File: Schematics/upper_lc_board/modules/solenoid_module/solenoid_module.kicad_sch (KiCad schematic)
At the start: 8 parts

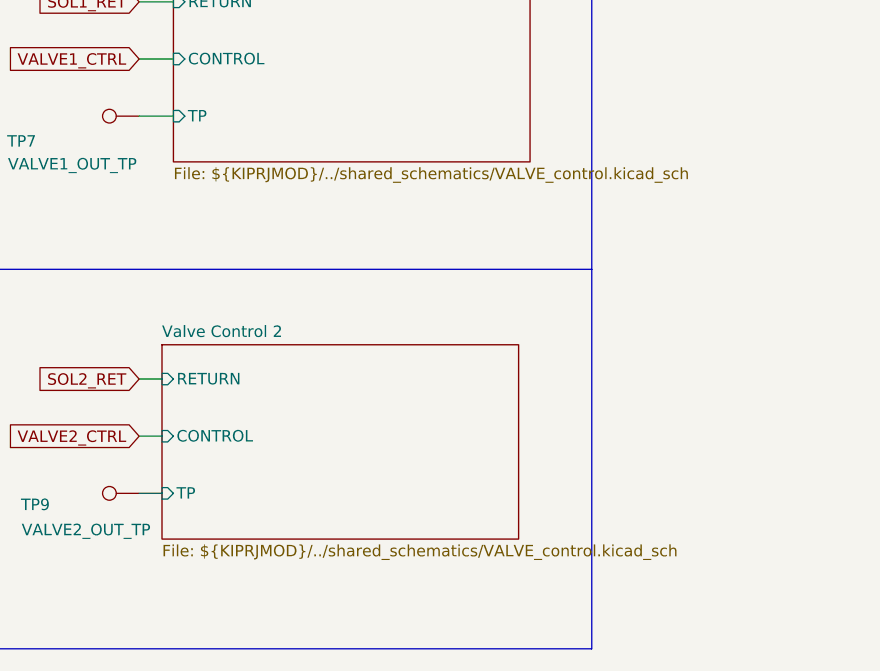
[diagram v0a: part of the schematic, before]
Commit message: fixed TC, PT, Valve schematic references and confirmed by updating PCB
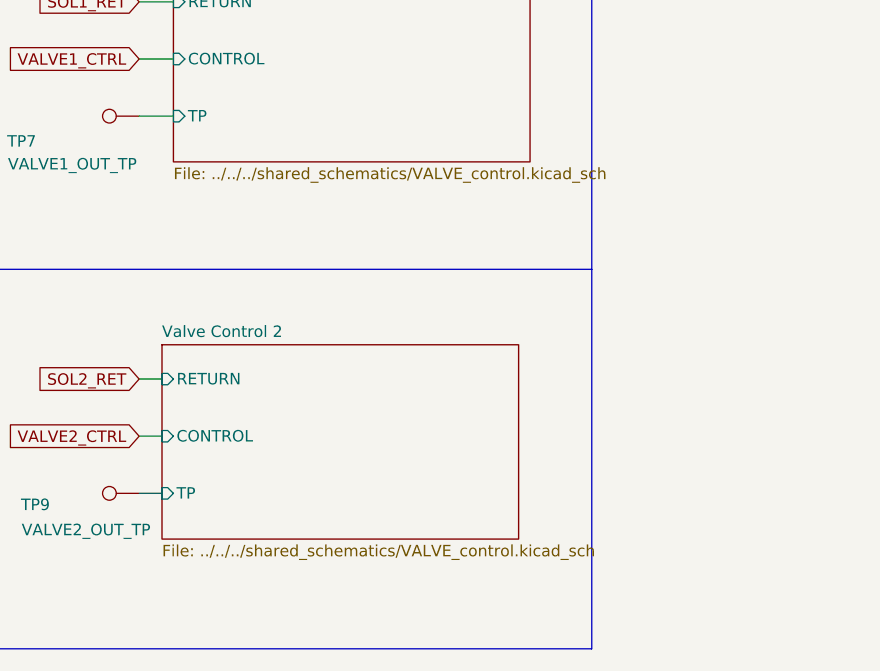
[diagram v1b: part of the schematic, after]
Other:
- sheet Valve Control 1: file ${KIPRJMOD}/../shared_schematics/VALVE_control.kicad_sch -> ../../../shared_schematics/VALVE_control.kicad_sch
- sheet Valve Control 2: file ${KIPRJMOD}/../shared_schematics/VALVE_control.kicad_sch -> ../../../shared_schematics/VALVE_control.kicad_sch
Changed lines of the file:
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@@
 			)
 		)
-		(property "Sheetfile" "${KIPRJMOD}/../shared_schematics/VALVE_control.kicad_sch"
+		(property "Sheetfile" "../../../shared_schematics/VALVE_control.kicad_sch"
 			(at 173.99 80.5946 0)
 			(effects
@@
 			)
 		)
-		(property "Sheetfile" "${KIPRJMOD}/../shared_schematics/VALVE_control.kicad_sch"
+		(property "Sheetfile" "../../../shared_schematics/VALVE_control.kicad_sch"
 			(at 172.72 122.5046 0)
 			(effects

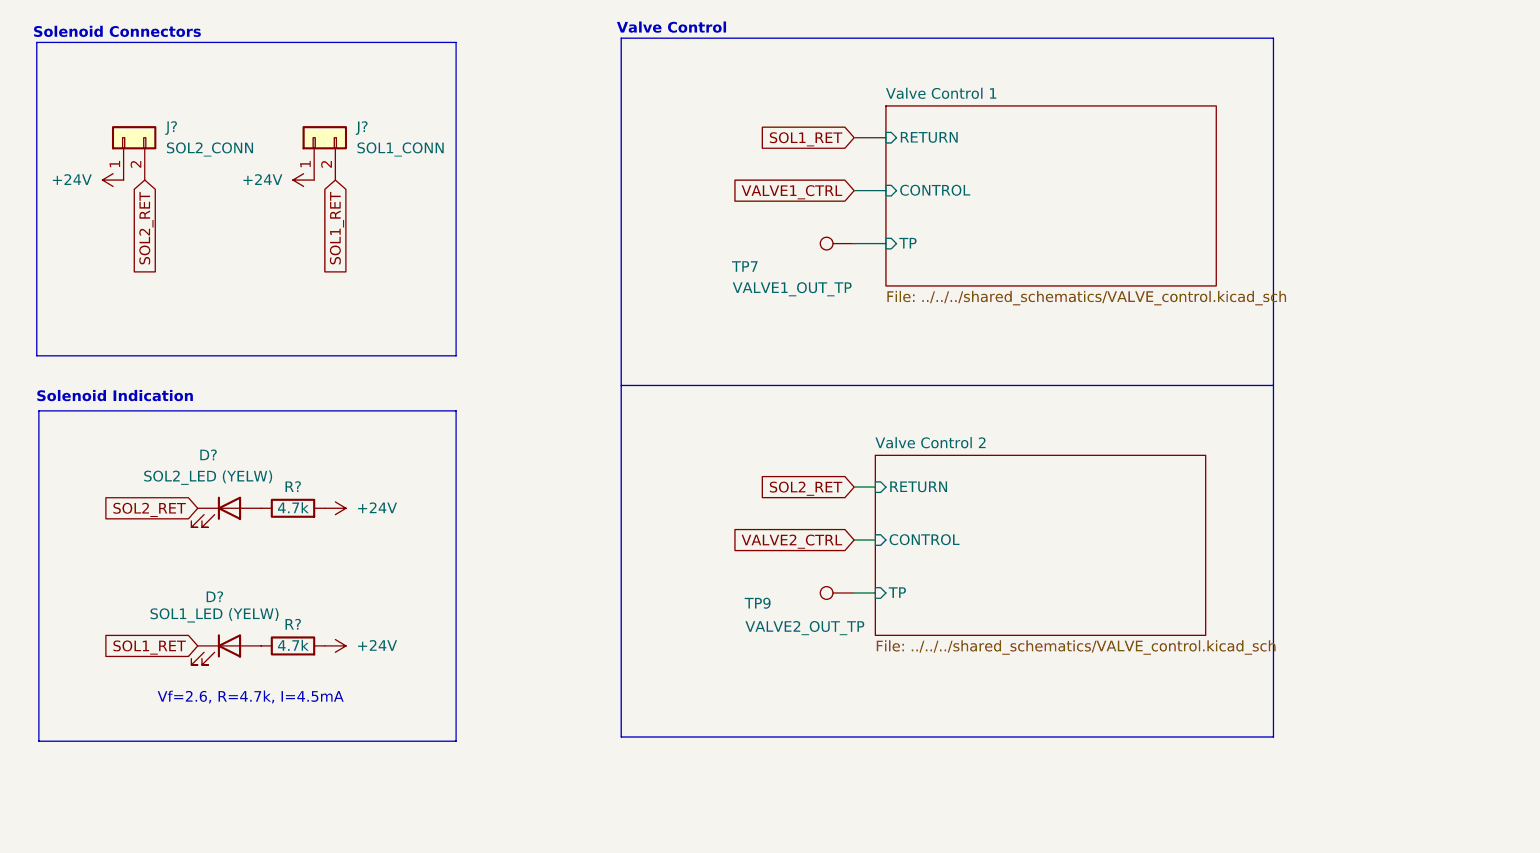
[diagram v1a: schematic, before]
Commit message: add references to caps, ferrite bead footprint, LDO datasheet
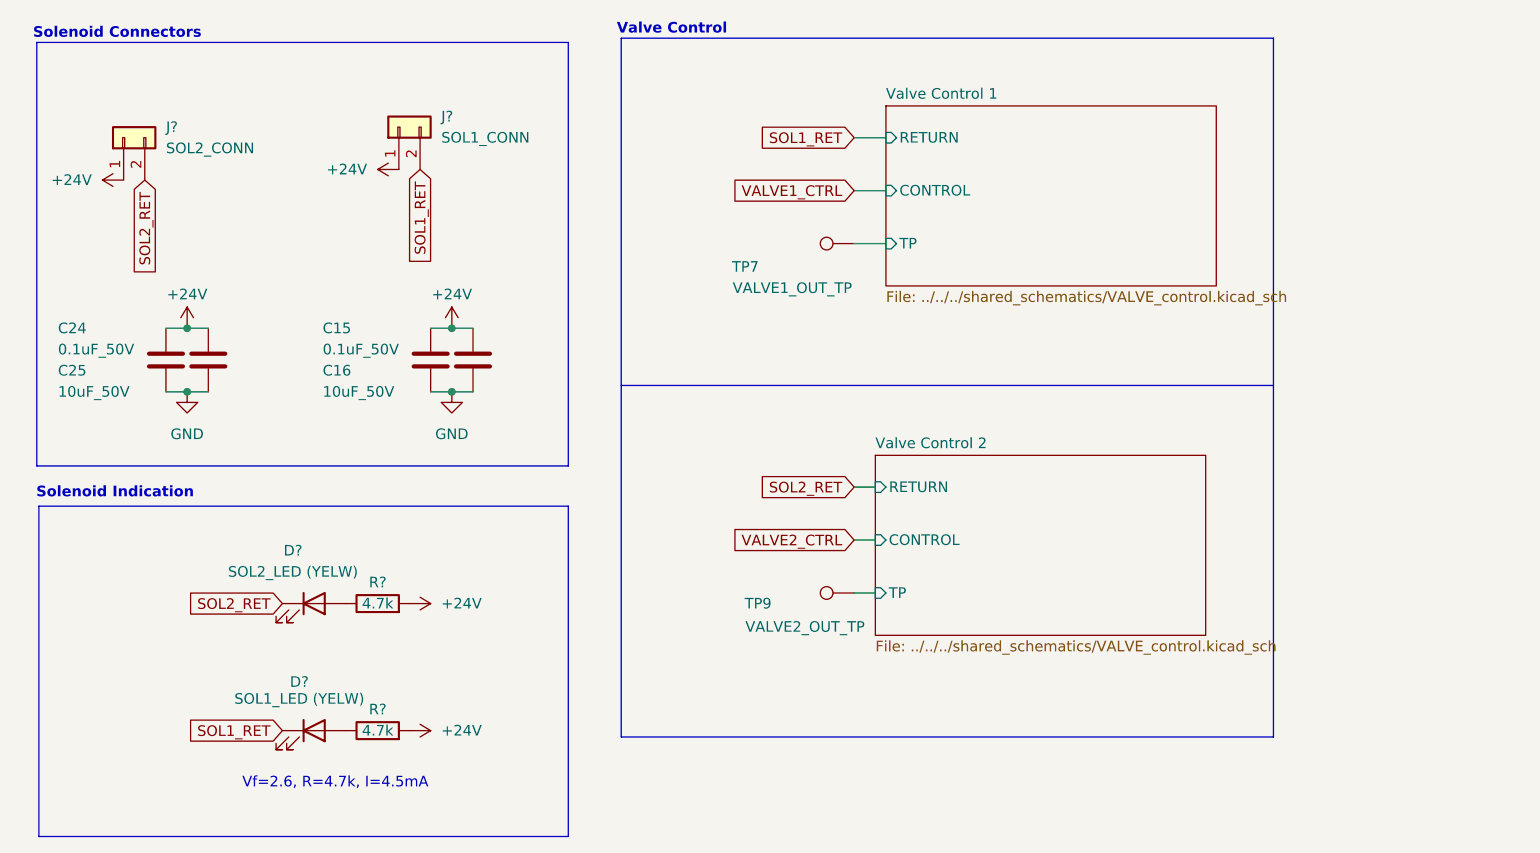
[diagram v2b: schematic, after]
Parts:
- added C15: 0.1uF_50V, Capacitor_SMD:C_0805_2012Metric, symbol Device:C
- added C16: 10uF_50V, Capacitor_SMD:CP_Elec_6.3x5.3, symbol Device:C
- added C24: 0.1uF_50V, Capacitor_SMD:C_0603_1608Metric, symbol Device:C
- added C25: 10uF_50V, Capacitor_SMD:C_1206_3216Metric, symbol Device:C
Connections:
- net +24V: now also C15.1, C16.1, C24.1, C25.1
- new net GND: C15.2, C16.2, C24.2, C25.2
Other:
- moved on the sheet: D?, J?, R?

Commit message: add decoupling, revise power circuitry (ferrite bead, LDO swap), merge shared-schemtic branch changes.
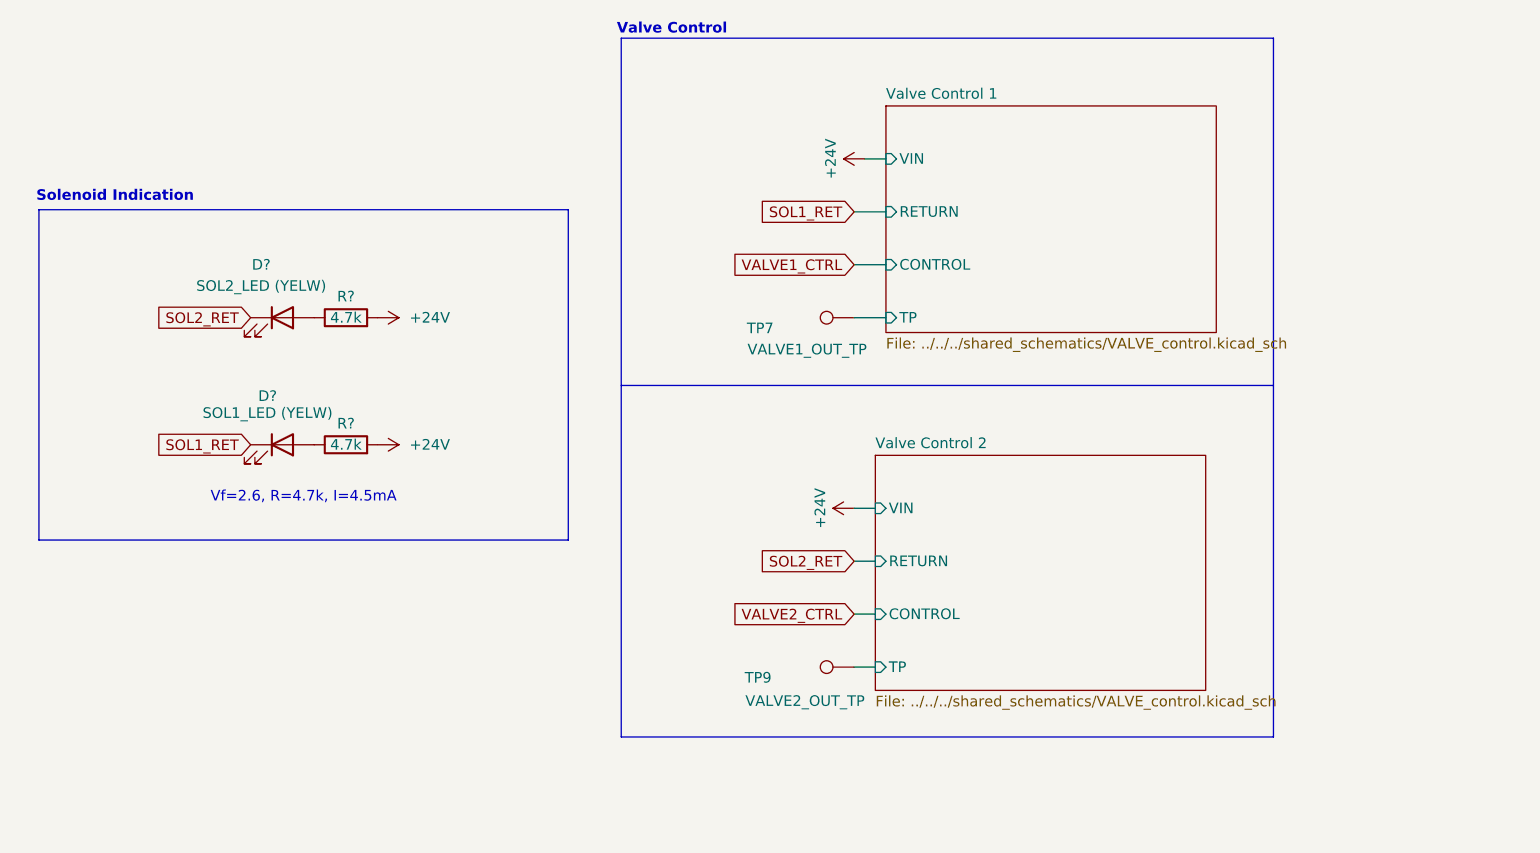
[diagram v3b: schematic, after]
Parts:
- removed C15: 0.1uF_50V, Capacitor_SMD:C_0805_2012Metric, symbol Device:C
- removed C16: 10uF_50V, Capacitor_SMD:CP_Elec_6.3x5.3, symbol Device:C
- removed C24: 0.1uF_50V, Capacitor_SMD:C_0603_1608Metric, symbol Device:C
- removed C25: 10uF_50V, Capacitor_SMD:C_1206_3216Metric, symbol Device:C
- removed J?: SOL1_CONN, CONNS:CONN02_530470260_MOL, symbol Connector_Generic:Conn_01x02
- removed J?: SOL2_CONN, CONNS:CONN02_530470260_MOL, symbol Connector_Generic:Conn_01x02
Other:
- sheet Valve Control 1 ports: added VIN; removed none
- sheet Valve Control 2 ports: added VIN; removed none
- note removed: "Solenoid Connectors"
- moved on the sheet: D?, R?, TP7, TP9
